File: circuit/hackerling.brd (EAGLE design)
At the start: 64.4 x 80 mm, 16 parts, among them IC1 MCP23017SP, IC2 MCP2300X/P, U2 LCD-16X2NOSILK, U3 ARDUINOR3-BPLACE

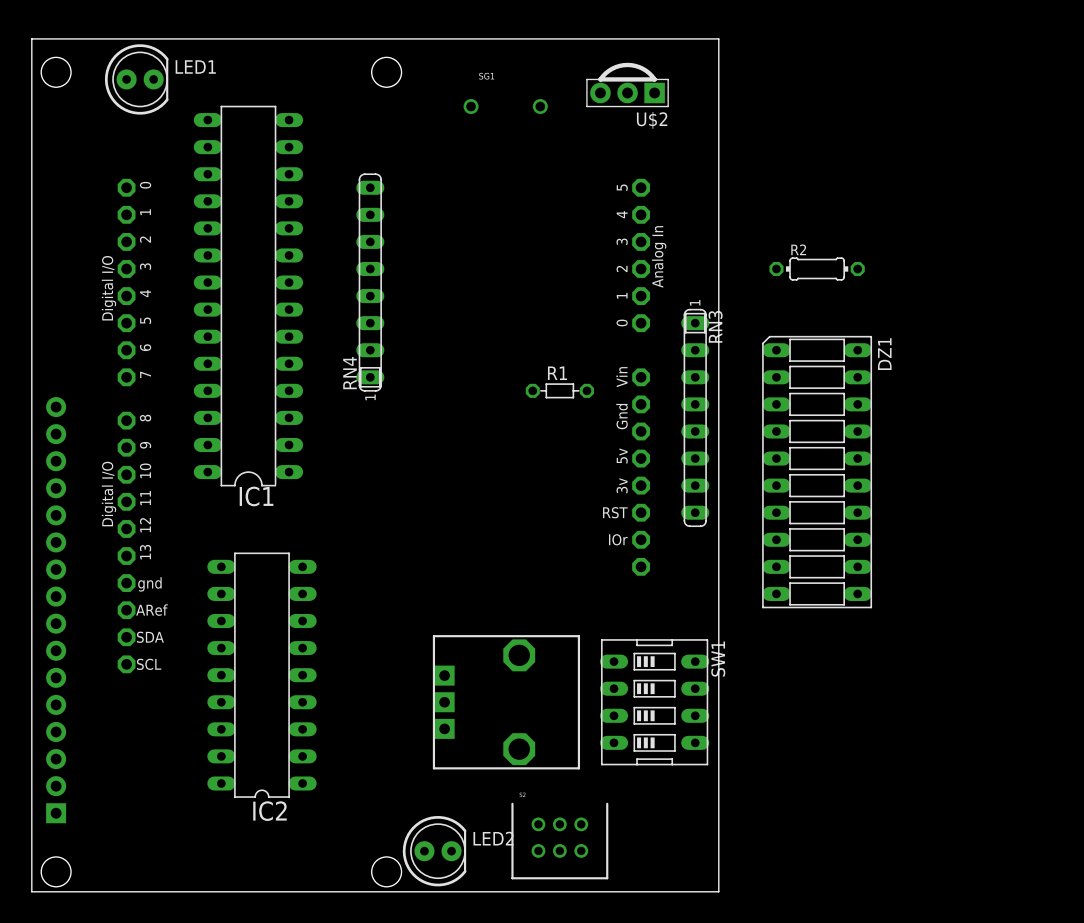
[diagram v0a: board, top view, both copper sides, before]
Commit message: arranging the hackerling circuit, added accelerometer layout
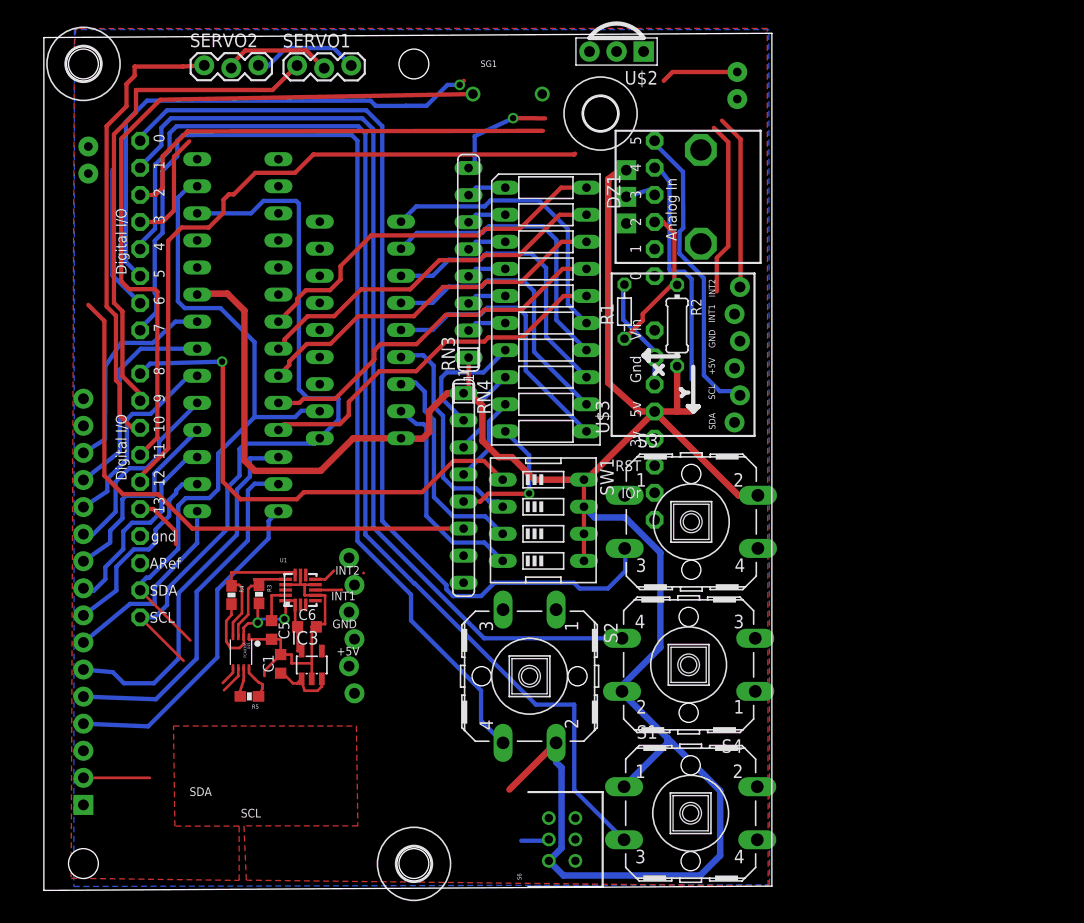
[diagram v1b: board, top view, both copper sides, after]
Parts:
- added C1: 1uF, resistor:C0603K
- added C5: 0.1uF, resistor:C0603K
- added C6: 4.7uF, resistor:C0603K
- added H1, H2, H3: MOUNT-HOLE3.2, holes:3,2
- added IC3: MIC5219BM5, v-reg-micrel:SOT23-5
- added R3, R4: 4k7, SparkFun:0603-RES
- added R5: 200K, SparkFun:0603-RES
- added S1, S3, S4: (no value), switch-omron:B3F-40XX
- added S6: SWITCH-DPDTOS, SparkFun:OS
- added SERVO1, SERVO2: (no value), SparkFun:1X03_LOCK
- added U$3, U$6: ACCELEROMETER, hackerscouts:ACCELEROMETER
- added U$5: PCA9306, hackerscouts:VSSOP-8
- added U1: MMA8452Q, hackerscouts:QFN-16(5X3)
- S2: value SWITCH-DPDTOS -> (none); device SparkFun:OS -> switch-omron:B3F-40XX
- moved LED2 72.7 mm to (5.30, 68.6), flipped to the bottom, turned to 90 degrees
- moved LED1 56.0 mm to (66.2, 75.6), flipped to the bottom, turned to 90 degrees
- moved U$1 50.4 mm to (62.8, 65.2)
- moved IC2 33.7 mm to (30.8, 52.7), flipped to the bottom
- moved DZ1 29.7 mm to (48.2, 54.6)
- moved RN3 25.8 mm to (41.0, 59.0), turned to 90 degrees
- moved RN4 21.2 mm to (40.5, 37.9), turned to 270 degrees
- moved SW1 20.0 mm to (48.0, 34.9)
- moved S2 15.4 mm to (46.7, 20.2), turned to 270 degrees
- moved R2 14.2 mm to (60.5, 53.1), turned to 270 degrees
- moved R1 9.59 mm to (55.6, 54.4), turned to 90 degrees
- moved U3 4.59 mm to (61.0, 6.95)
- moved U$2 4.02 mm to (54.9, 78.8)
- moved IC1 3.80 mm to (19.3, 52.2), flipped to the bottom
- moved U2 2.68 mm to (20.3, 40.1)
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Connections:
- removed net IR_OUT: LED1.K, LED2.K, U3.D5
- removed net N$11 (its old number): IC1.26, U2.4
- removed net N$24 (its old number): DZ1.7, RN3.8
- removed net N$28: SW1.3, U3.D1
- removed net N$29: SW1.4, U3.D0
- new net 3.3V: C6.1, IC3.5, R3.2, R4.2, U$5.P$2, U1.1, U1.14
- new net 5V: R5.2, U$5.P$7
- new net A_INT1: U$3.5, U1.11, U3.D3
- new net A_INT2: U$3.6, U1.9, U3.D2
- new net BTN1: S1.3, U3.D4
- new net BTN2: S2.4, U3.D7
- new net BTN3: S3.3, U3.D0
- new net BTN4: S4.4, U3.D1
- new net DIP1: IC2.15, SW1.2
- new net DIP2: IC2.16, SW1.3
- new net DIP3: IC2.17, SW1.4
- new net IR_OUT1: LED1.K, U3.D5
- new net IR_OUT2: LED2.K, U3.D6
- new net N$10: IC1.28, U2.4
- new net N$17: DZ1.10, RN4.5
- new net SCL1: U$3.2, U3.A5
- new net SCL_3: R3.1, U$5.P$3, U1.4
- new net SDA1: U$3.1, U3.A4
- new net SDA_3: R4.1, U$5.P$4, U1.6
- new net SVO1: SERVO1.1, U3.D9
- new net SVO2: SERVO2.1, U3.D10
- new net SWITCH: S6.2, U3.D13
- net GND: now also C1.2, C5.2, C6.2, IC3.2, SERVO1.3, SERVO2.3, U$3.4, U$5.P$1, U1.10, U1.12, U1.5, U1.7
- net IR_IN: now also U3.D12; no longer U3.D7
- net N$12: now also DZ1.7; no longer DZ1.8
- net N$13: now also DZ1.8; no longer DZ1.9
- net N$14: now also DZ1.9; no longer DZ1.10
- net N$16: now also RN3.8; no longer RN4.5
- net N$18: now also RN3.7; no longer RN3.2
- net N$19: now also RN3.6; no longer RN3.3
- net N$20: now also RN3.5; no longer RN3.4
- net N$21: now also RN3.4; no longer RN3.5
- net N$22: now also RN3.3; no longer RN3.6
- net N$23: now also RN3.2; no longer RN3.7
- net N$25: now also C5.1, U1.2; no longer U3.D12
- net N$26: now also U3.D8; no longer U3.D3
- net N$27: now also R5.1, U$5.P$8; no longer SW1.2, U3.D2
- net N$9: now also IC1.26; no longer IC1.28
- net SCL: now also U$5.P$6
- net SDA: now also U$5.P$5
- net VCC: now also C1.1, IC3.1, IC3.3, S1.1, S2.2, S3.2, S4.2, S6.1, SERVO1.2, SERVO2.2, SW1.5, SW1.6, SW1.7, SW1.8, U$3.3
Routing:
- net VCC: track 0.00 -> 229.3 mm
- net BTN1: track 0.00 -> 109.7 mm
- net BTN2: track 0.00 -> 98.8 mm
- net BTN3: track 0.00 -> 91.3 mm
- net BTN4: track 0.00 -> 90.2 mm
- net SCL: track 0.00 -> 72.9 mm
- net N$15: track 0.00 -> 67.7 mm
- net IR_IN: track 0.00 -> 66.0 mm
- net SDA: track 0.00 -> 64.8 mm
- net A_INT2: track 0.00 -> 60.4 mm
- net IR_OUT1: track 0.00 -> 56.0 mm, vias 0 -> 1
- net GND: track 0.00 -> 53.7 mm
- net N$24: track 0.00 -> 52.4 mm
- net N$26: track 0.00 -> 48.5 mm, vias 0 -> 1
- net SVO1: track 0.00 -> 47.1 mm
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- added copper zone on layer 1, net GND
- added copper zone on layer 16, net GND
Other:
- board size 64.4 x 80 mm -> 68.3 x 80.4 mm
- board text added: "+5V"
- board text added: "GND"
- board text added: "INT1"
- board text added: "INT2"
- board text added: "SCL"
- board text added: "SDA"

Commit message: still arranging, about to rotate and shift parts
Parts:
- moved U$6 64.0 mm to (88.9, 25.9), flipped to the top, turned to 0 degrees
- moved U$3 44.1 mm to (24.8, 25.3), flipped to the bottom, turned to 270 degrees
- moved R2 22.4 mm to (82.2, 47.3)
- moved R1 22.0 mm to (77.6, 53.7)
- moved R5 13.1 mm to (25.9, 30.3), turned to 0 degrees
- moved R4 11.0 mm to (27.7, 21.5), turned to 90 degrees
- moved IC3 9.08 mm to (20.2, 28.0), turned to 180 degrees
- moved U$5 8.41 mm to (26.8, 26.8), turned to 0 degrees
- moved U1 8.32 mm to (21.2, 21.0), turned to 180 degrees
- moved R3 7.56 mm to (25.1, 21.4), turned to 90 degrees
- moved C1 6.54 mm to (23.1, 27.9), turned to 270 degrees
- moved C6 5.20 mm to (20.6, 24.4), turned to 180 degrees
- moved U$1 3.19 mm to (63.0, 62.0)
- moved LED1 2.37 mm to (65.5, 73.4)
- moved S2 1.69 mm to (45.3, 21.1), turned to 180 degrees
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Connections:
- net SCL: now also U$3.2
- net SCL1: no longer U$3.2
- net SDA: now also U$3.1
- net SDA1: no longer U$3.1
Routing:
- net SWITCH: track 8.04 -> 65.2 mm, vias 0 -> 1
- net A_INT2: track 60.4 -> 13.4 mm
- net SCL1: track 27.8 -> 0.00 mm
- net SDA1: track 22.2 -> 0.00 mm
- net SCL: track 72.9 -> 91.7 mm, vias 0 -> 1
- net SDA: track 64.8 -> 79.9 mm, vias 0 -> 1
- net TEMP: track 14.6 -> 0.00 mm
- net BTN2: track 98.8 -> 92.0 mm
- net A_INT1: track 29.5 -> 24.9 mm
- net N$16: track 10.7 -> 12.8 mm
- net VCC: track 229.3 -> 230.8 mm
- net POT: track 2.96 -> 4.21 mm
- net N$27: track 3.40 -> 2.82 mm
- net GND: track 53.7 -> 53.5 mm, vias 0 -> 1

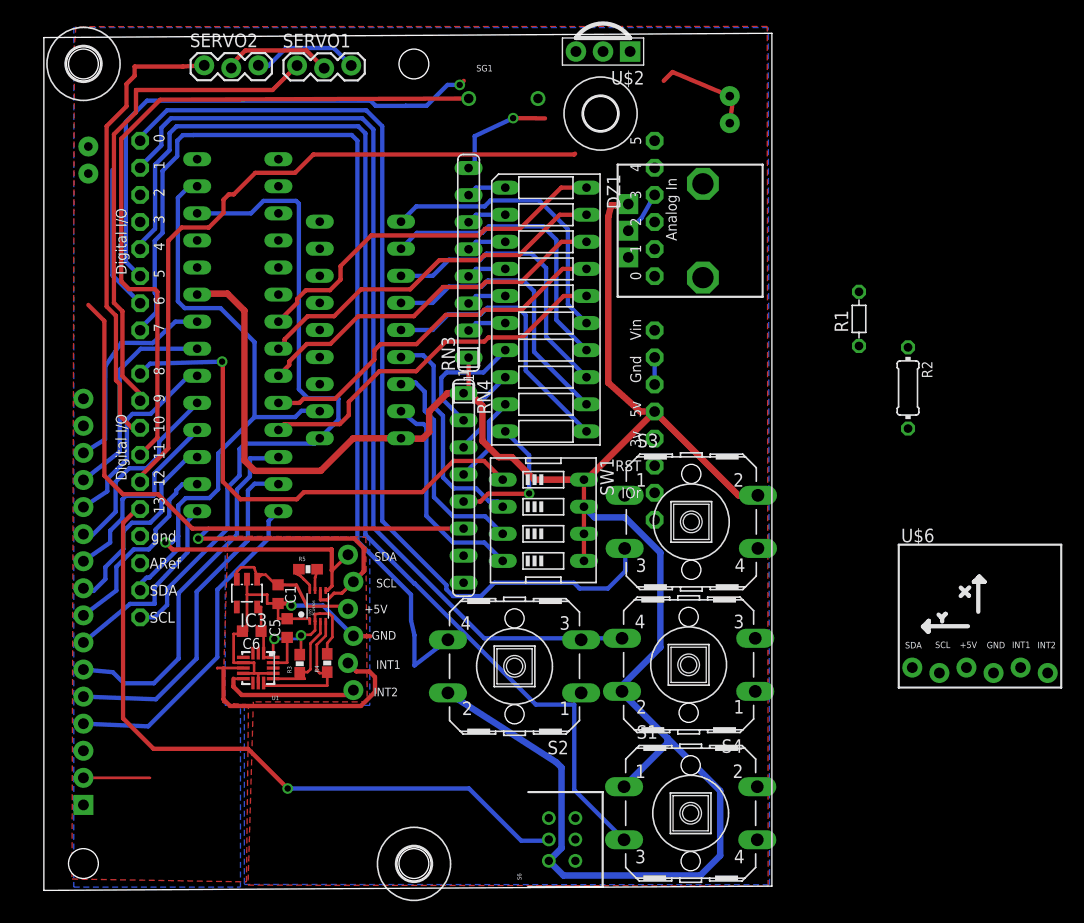
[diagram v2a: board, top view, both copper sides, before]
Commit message: circuit state as of barebones order BOM is out of date still.... Just copied hackerling_a back to hackerling.
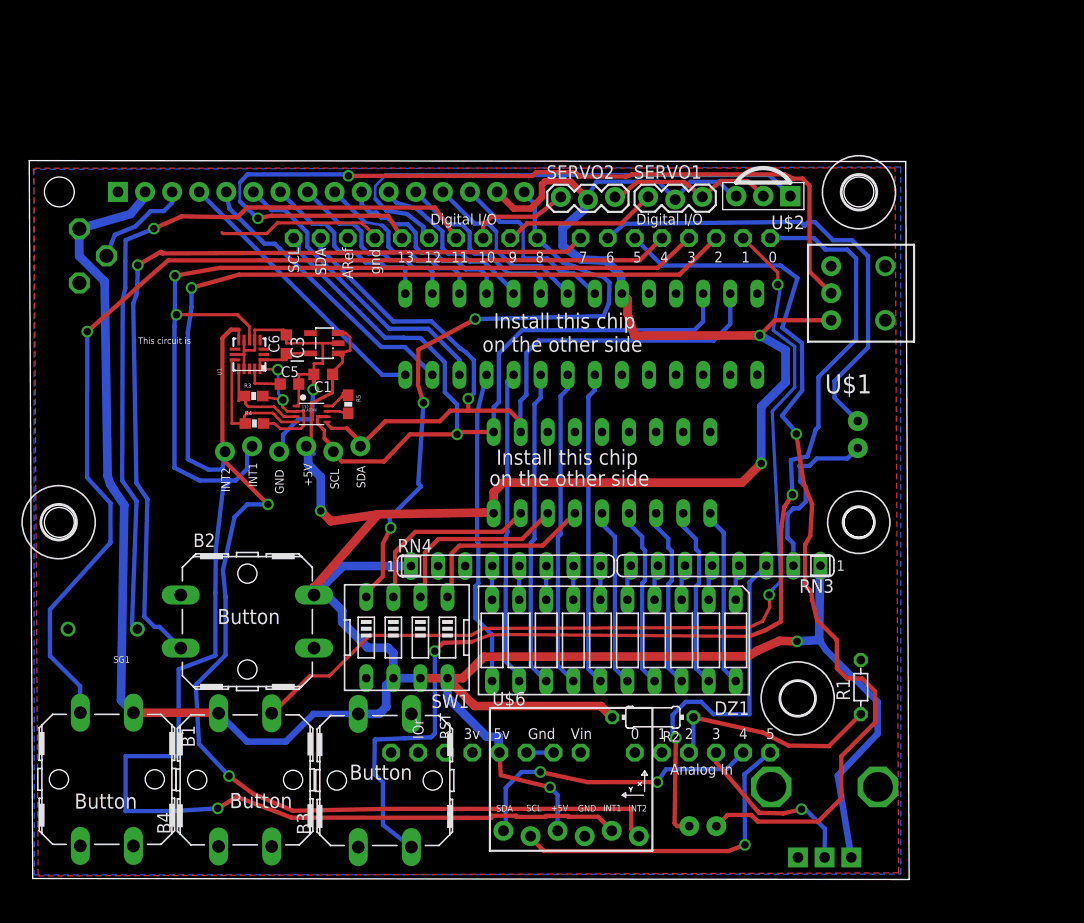
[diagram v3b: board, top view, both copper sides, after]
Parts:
- removed S1, S2, S3, S4: (no value), switch-omron:B3F-40XX
- removed S6: SWITCH-DPDTOS, SparkFun:OS
- added B1, B2, B3, B4: (no value), hackerscouts:SWITCH_B3F-4000
- added H4: MOUNT-HOLE2.8, holes:2,8
- added U$7: POT, hackerscouts:ALS_POT
- added U$8: SML_POT, hackerscouts:SML_POT
- U$1: value (none) -> SWITCH_B13EH; device SparkFun:ALPS_POT -> hackerscouts:SWITCH_B13EH
- moved LED2 76.6 mm to (77.5, 42.9)
- moved H3 73.7 mm to (77.6, 65.6), turned to 90 degrees
- moved LED1 67.3 mm to (62.9, 6.16), turned to 180 degrees
- moved SG1 62.4 mm to (6.65, 24.6), turned to 180 degrees
- moved H2 57.9 mm to (71.8, 18.1), turned to 270 degrees
- moved U3 55.3 mm to (5.76, 10.5), turned to 0 degrees
- moved H1 46.2 mm to (2.52, 34.7), turned to 270 degrees
- moved U$6 41.3 mm to (50.6, 10.6)
- moved R2 39.1 mm to (58.2, 16.4), turned to 180 degrees
- moved RN3 37.3 mm to (65.1, 30.6), turned to 180 degrees
- moved SERVO2 35.7 mm to (49.6, 65.0)
- moved SERVO1 35.2 mm to (57.8, 65.1)
- moved R1 34.5 mm to (77.8, 19.2)
- moved IC1 32.2 mm to (51.5, 52.3), turned to 180 degrees
- moved DZ1 31.7 mm to (54.6, 23.6), turned to 180 degrees
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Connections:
- removed net A: U2.15
- removed net K: U2.16
- removed net N$14: DZ1.9, RN4.4
- removed net N$19: DZ1.2, RN3.6
- removed net N$24: LED2.A, RN4.6
- removed net N$26: SW1.1, U3.D8
- removed net VSS: U2.1
- new net BACKLIGHT: SW1.4, U2.16, U3.D8
- new net N$28: DZ1.7, RN4.7
- new net N$29: DZ1.8, RN4.6
- new net N$30: DZ1.9, RN4.5
- new net N$31: DZ1.10, RN4.4
- net A_INT1: now also U$6.5
- net A_INT2: now also U$6.6
- net BARGRAPH0: now also IC2.10; no longer IC1.21
- net BARGRAPH1: now also IC2.11; no longer IC1.22
- net BARGRAPH2: now also IC2.12; no longer IC1.23
- net BARGRAPH3: now also IC2.13; no longer IC1.24
- net BARGRAPH4: now also IC2.14; no longer IC1.25
- net BARGRAPH5: now also IC1.21; no longer IC2.10
- net BARGRAPH6: now also IC1.22; no longer IC2.11
- net BARGRAPH7: now also IC1.23; no longer IC2.12
- net BARGRAPH8: now also IC1.24; no longer IC2.13
- net BARGRAPH9: now also IC1.25; no longer IC2.14
- net BTN1: now also B1.3; no longer S1.3
- net BTN2: now also B2.3; no longer S2.4
- net BTN3: now also B3.3; no longer S3.3
- net BTN4: now also B4.4; no longer S4.4
- net DIP1: now also SW1.1; no longer SW1.2
- net DIP2: now also SW1.2; no longer SW1.3
- net DIP3: now also SW1.3; no longer SW1.4
- net GND: now also SW1.5, U$1.3, U$6.4, U$7.P$1, U$8.E, U2.1; no longer U$1.P$3, U2.2
- net N$12: now also LED2.A, RN3.2; no longer DZ1.7, RN4.2
- net N$13: now also U$8.S, U2.3; no longer DZ1.8, RN4.3
- net N$16: now also RN3.3; no longer RN3.8
- net N$17: now also DZ1.2, RN3.5; no longer DZ1.10, RN4.5
- net N$18: now also RN3.4; no longer RN3.7
- net N$20: now also RN3.6; no longer RN3.5
- net N$21: now also RN3.7; no longer RN3.4
- net N$22: now also RN3.8; no longer RN3.3
- net N$23: now also RN4.8; no longer RN3.2
- net POT: now also U$7.P$2; no longer U$1.P$2
- net SCL1: now also U$6.2
- net SDA1: now also U$6.1
- net SWITCH: now also U$1.2; no longer S6.2
- net VCC: now also B1.1, B2.2, B3.2, B4.2, U$1.1, U$6.3, U$7.P$3, U$8.A, U2.15, U2.2; no longer S1.1, S2.2, S3.2, S4.2, S6.1, SW1.5, U$1.P$1
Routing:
- net A_INT2: track 13.4 -> 164.1 mm, vias 0 -> 3
- net VCC: track 230.8 -> 379.8 mm, vias 0 -> 5
- net A_INT1: track 24.9 -> 172.0 mm, vias 0 -> 3
- net BACKLIGHT: track 0.00 -> 59.8 mm, vias 0 -> 3
- net N$24: track 52.4 -> 0.00 mm
- net N$26: track 48.5 -> 0.00 mm, vias 1 -> 0
- net SVO2: track 43.3 -> 9.61 mm
- net SVO1: track 47.1 -> 15.0 mm
- net SCL1: track 0.00 -> 30.6 mm, vias 0 -> 1
- net IR_OUT2: track 13.6 -> 44.2 mm
- net IR_OUT1: track 55.7 -> 86.2 mm
- net SDA1: track 0.00 -> 28.4 mm, vias 0 -> 2
- net N$16: track 12.8 -> 34.6 mm
- net TEMP: track 0.00 -> 20.9 mm
- net SWITCH: track 65.2 -> 84.2 mm, vias 1 -> 2
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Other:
- board size 68.3 x 80.4 mm -> 82.5 x 67.4 mm
- board text added: "Button"
- board text added: "Install this chip"
- board text added: "Place MCP2300 here."
- board text added: "Place MCP23017 here."
- board text added: "Solder on the other side."
- board text added: "Step 1:"
- board text added: "Step 2:"
- board text added: "This circuit is"
- board text added: "match up the indent"
- board text added: "on the other side"

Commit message: adding instruction steps
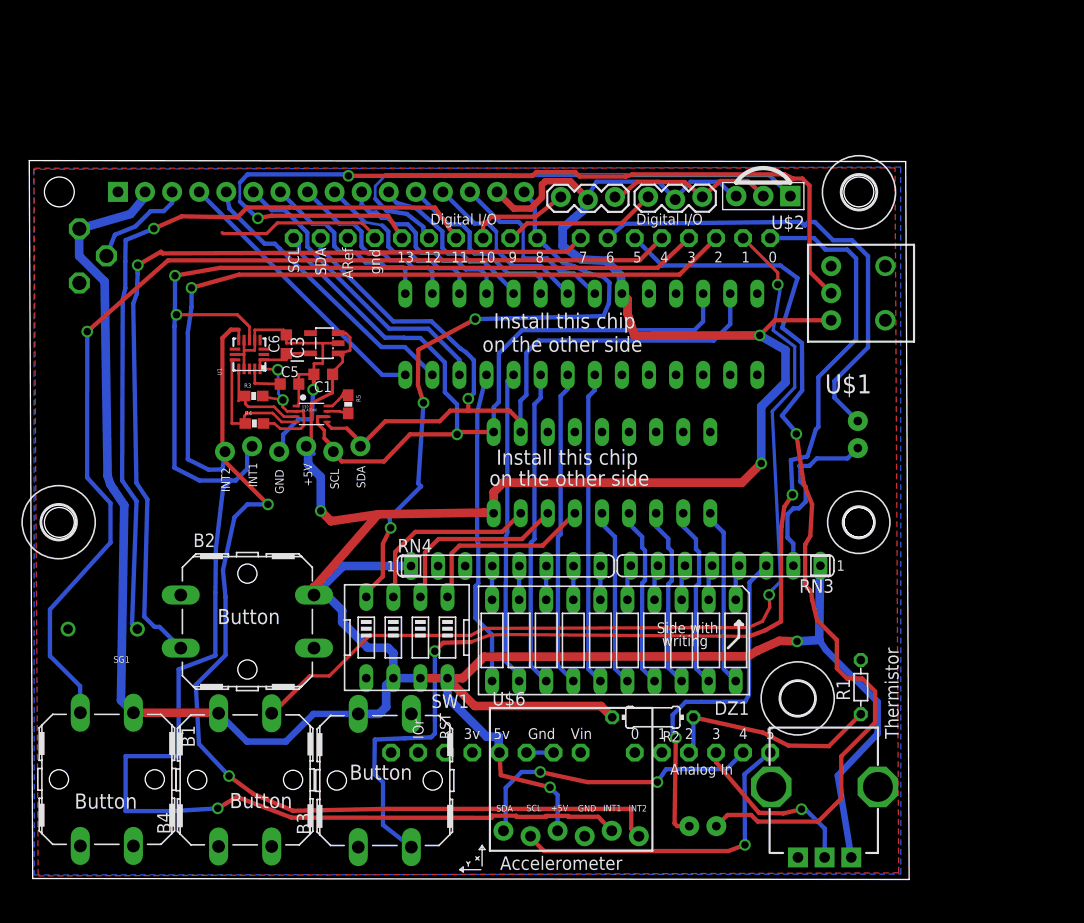
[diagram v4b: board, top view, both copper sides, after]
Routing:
- net N$16: track 34.6 -> 32.6 mm
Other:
- board text added: "8:"
- board text added: "??:"
- board text added: "Accelerometer"
- board text added: "Headers"
- board text added: "IR reciever"
- board text added: "If not, install a"
- board text added: "Install 4 buttons"
- board text added: "Install LED"
- board text added: "Install resistor array"
- board text added: "Install switch here"
- board text added: "Leave .5" out"
- board text added: "Side with"
- board text added: "Solder on the"
- board text added: "Step"
- board text added: "Step 0:"
- board text added: "Step 10:"
- board text added: "Step 11:"
- board text added: "Step 3: Install Arduino headers. Solder other side."
- board text added: "Step 4:"
- board text added: "Step 5:"
- board text added: "Step 6:"
- board text added: "Step 7:"
- board text added: "Step 9: Servo headers."
- board text added: "Step ??"
- board text added: "Step ??:"
- board text added: "Thermistor"
- board text added: "This circuit may"
- board text added: "arrow"
- board text added: "be pre-installed"
- board text added: "daughter board"
- board text added: "goes"
- board text added: "here"
- board text added: "only use 5 pins"
- board text added: "other side."
- board text added: "potentiometer"
- board text added: "writing"
- board text removed: "This circuit is"
